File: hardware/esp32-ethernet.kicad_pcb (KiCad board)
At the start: 4 copper layers, 80 x 40 mm, 126 parts, among them J101 USB-C-2, P101 EXT_HEADER, P201 CON-SENSOR2, P202 CON-SENSOR2, P203 CON-SENSOR2, P204 CON-SENSOR2, P205 CON-SENSOR2, P206 CON-SENSOR2, P301 POE, P302 RJPSL-001TA1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

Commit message: moure routing
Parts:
- moved D104 24.5 mm to (154.3, 143.3), turned to 90 degrees
- moved R110 10.9 mm to (182.2, 127.2), turned to 90 degrees
- moved C115 10.8 mm to (181.2, 127.2), turned to 90 degrees
- moved R102 8.41 mm to (156.6, 142.5), turned to 270 degrees
- moved RP101 6.74 mm to (155.0, 146.3), turned to 0 degrees
- moved R112 5.61 mm to (153.7, 140.6), turned to 0 degrees
- moved R114 4.92 mm to (149.3, 143.1), turned to 90 degrees
- moved R1 3.40 mm to (133.7, 130.1)
- moved C306 3.30 mm to (191.4, 132.6), turned to 270 degrees
- moved R107 3.23 mm to (169.0, 150.4), turned to 90 degrees
- moved L301 1.80 mm to (185.1, 135.4)
- moved C301 1.70 mm to (182.1, 135.4)
- moved C302 1.13 mm to (179.7, 134.1)
- moved C303 1.11 mm to (189.9, 135.8)
- moved C305 1.10 mm to (182.3, 134.3)
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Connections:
- D104 pad 1: ESP_IO0_AUTO -> ESP_IO0_KEY
- D104 pad 2: ESP_IO0_KEY -> ESP_IO0_AUTO
- RP101 pad 1: B0-MISO -> B0-CLK
- RP101 pad 2: B0-CLK -> B0-MISO
- RP101 pad 7: Net-(RP101-Pad7) -> Net-(R102-Pad1)
- RP101 pad 8: Net-(R102-Pad1) -> Net-(RP101-Pad8)
- U104 pad 13: Net-(RP101-Pad7) -> Net-(RP101-Pad8)
- U104 pad 8: B-CS0 -> B-CS1
- U104 pad 9: B-CS1 -> B-CS0
- U204 pad 10: B0-CS5 -> B0-CS0
- U204 pad 11: B0-CS4 -> B0-CS1
- U204 pad 12: B0-CS3 -> B0-CS2
- U204 pad 13: B0-CS2 -> B0-CS3
- U204 pad 14: B0-CS1 -> B0-CS4
- U204 pad 15: B0-CS0 -> B0-CS5
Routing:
- net B-CS2: track 0.00 -> 36.4 mm, vias 0 -> 2
- net Net-(Q101-PadE): track 1.61 -> 32.1 mm, vias 0 -> 2
- net ESP_TXD: track 1.72 -> 26.5 mm
- net B0-CS2: track 5.79 -> 29.6 mm, vias 2 -> 3
- net B0-CS4: track 8.26 -> 31.8 mm, vias 0 -> 2
- net ESP_ADC_5V: track 1.04 -> 24.3 mm, vias 0 -> 2
- net Net-(Q102-PadE): track 2.43 -> 25.4 mm, vias 1 -> 2
- net B0-CS5: track 19.8 -> 41.9 mm, vias 2 -> 3
- net ESP_ADC_VUSB: track 1.08 -> 23.0 mm, vias 0 -> 2
- net ESP_RXD: track 2.70 -> 23.6 mm, vias 0 -> 2
- net 3V3: track 34.9 -> 55.6 mm, vias 33 -> 40
- net B0-CS3: track 21.8 -> 40.9 mm, vias 0 -> 2
- net B-CS1: track 0.00 -> 16.2 mm, vias 0 -> 2
- net Net-(P302-Pad6): track 0.00 -> 15.3 mm
- net B-CS0: track 0.00 -> 14.7 mm, vias 0 -> 2
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
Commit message: more routing
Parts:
- moved R310 0.20 mm to (177.4, 126.5)
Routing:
- net RMII_RXD1: track 0.00 -> 37.5 mm, vias 0 -> 2
- net ESP_IO0: track 0.65 -> 35.4 mm, vias 1 -> 3
- net RMII_RXD0: track 0.00 -> 34.6 mm, vias 0 -> 2
- net RMII_CRS: track 0.65 -> 33.3 mm, vias 1 -> 2
- net LED_GREEN: track 2.88 -> 27.4 mm
- net RMII_MDC: track 0.70 -> 16.9 mm, vias 1 -> 2
- net RMII_MDIO: track 0.80 -> 14.6 mm, vias 1 -> 2
- net Net-(R304-Pad1): track 1.16 -> 7.42 mm, vias 1 -> 2
- net GND: track 114.7 -> 120.6 mm, vias 119 -> 129
- net Net-(R306-Pad1): track 1.08 -> 6.58 mm, vias 1 -> 2
- net RMII_TX_EN: track 0.00 -> 3.11 mm
- net RMII_TXD0: track 0.00 -> 1.81 mm
- net RMII_TXD1: track 0.00 -> 1.61 mm
- net LED_BLUE: track 0.00 -> 1.41 mm, vias 0 -> 1

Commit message: routing finished
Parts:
- moved R315 0.64 mm to (175.5, 152.6)
- moved C312 0.50 mm to (175.5, 149.9)
- moved C313 0.50 mm to (175.5, 151.1)
- moved R316 0.50 mm to (175.5, 153.8)
- moved C303 0.20 mm to (189.9, 136.1)
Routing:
- net GND: track 120.6 -> 249.4 mm, vias 129 -> 188
- net LED_BLUE: track 1.41 -> 45.2 mm, vias 1 -> 2
- net Net-(P301-Pad3): track 0.00 -> 30.8 mm, vias 0 -> 2
- net Net-(P301-Pad4): track 0.00 -> 28.1 mm, vias 0 -> 2
- net yellowLED: track 0.58 -> 26.9 mm, vias 1 -> 2
- net Net-(P301-Pad1): track 0.00 -> 21.7 mm, vias 0 -> 2
- net ESP_EN: track 0.00 -> 17.6 mm, vias 0 -> 2
- net Net-(P301-Pad2): track 0.00 -> 15.2 mm, vias 0 -> 2
- net SHD: track 0.00 -> 14.2 mm, vias 0 -> 12
- net 3V3: track 55.6 -> 68.9 mm, vias 40 -> 49
- net LED_GREEN: track 27.4 -> 38.7 mm
- net RMII_RESET: track 1.46 -> 10.7 mm, vias 0 -> 2
- net ESP_IO0: track 35.4 -> 41.9 mm
- net Net-(C312-Pad2): track 0.00 -> 5.84 mm
- net Net-(C313-Pad2): track 0.00 -> 5.51 mm
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- added copper zone on B.Cu, net GND
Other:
- outline, holes or cut-outs redrawn

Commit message: improve layer design
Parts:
- P301: footprint kicad-libraries:pin_array_4x1 -> kicad-libraries:pin_array_5x1
- moved D101 2.90 mm to (171.8, 161.3)
- moved R115 2.90 mm to (171.8, 158.8)
- moved P301 1.20 mm to (181.1, 160.7)
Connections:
- P101 pad 6: Net-(P101-Pad6) -> GND
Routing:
- net GND: track 249.4 -> 258.8 mm, vias 188 -> 190
- net SHD: track 14.2 -> 20.8 mm
- net Net-(P301-Pad4): track 28.1 -> 29.3 mm
- net Net-(P301-Pad1): track 21.7 -> 22.8 mm
- net LED_BLUE: track 45.2 -> 44.1 mm
- net Net-(P301-Pad3): track 30.8 -> 31.8 mm
- net Net-(P301-Pad2): track 15.2 -> 16.2 mm
- net Net-(P101-Pad6): track 0.71 -> 0.00 mm
- added copper zone on F.Cu, net SHD
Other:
- board text added: "IO35 IO34 GND IO15 IO2 3V3 GND 5V"
- board text removed: "IO35 IO22 IO21 IO15 IO5 3V3 GND 5V"

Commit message: version 1.0
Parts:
- U204: value SN74LV138AD -> SN74LV138APW

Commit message: fix port description
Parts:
- added Fiducial_Mark: VAL**, kicad-libraries:Fiducial_Mark, F.Cu at (188.0, 124.8)
- added Fiducial_Mark: VAL**, kicad-libraries:Fiducial_Mark, F.Cu at (119.3, 158.7)
- added Fiducial_Mark: VAL**, kicad-libraries:Fiducial_Mark, F.Cu at (174.3, 157.7)
- added Fiducial_Mark: VAL**, kicad-libraries:Fiducial_Mark, F.Cu at (119.3, 129.7)
- added G***: LOGO, kicad-libraries:Logo_31x31, F.Cu at (135.6, 142.8)
- added VAL: CE_5mm, kicad-libraries:CE_5mm, B.Cu at (162.8, 143.7)
- added VAL: WEEE_7mm, kicad-libraries:WEEE_7mm, B.Cu at (170.8, 143.7)

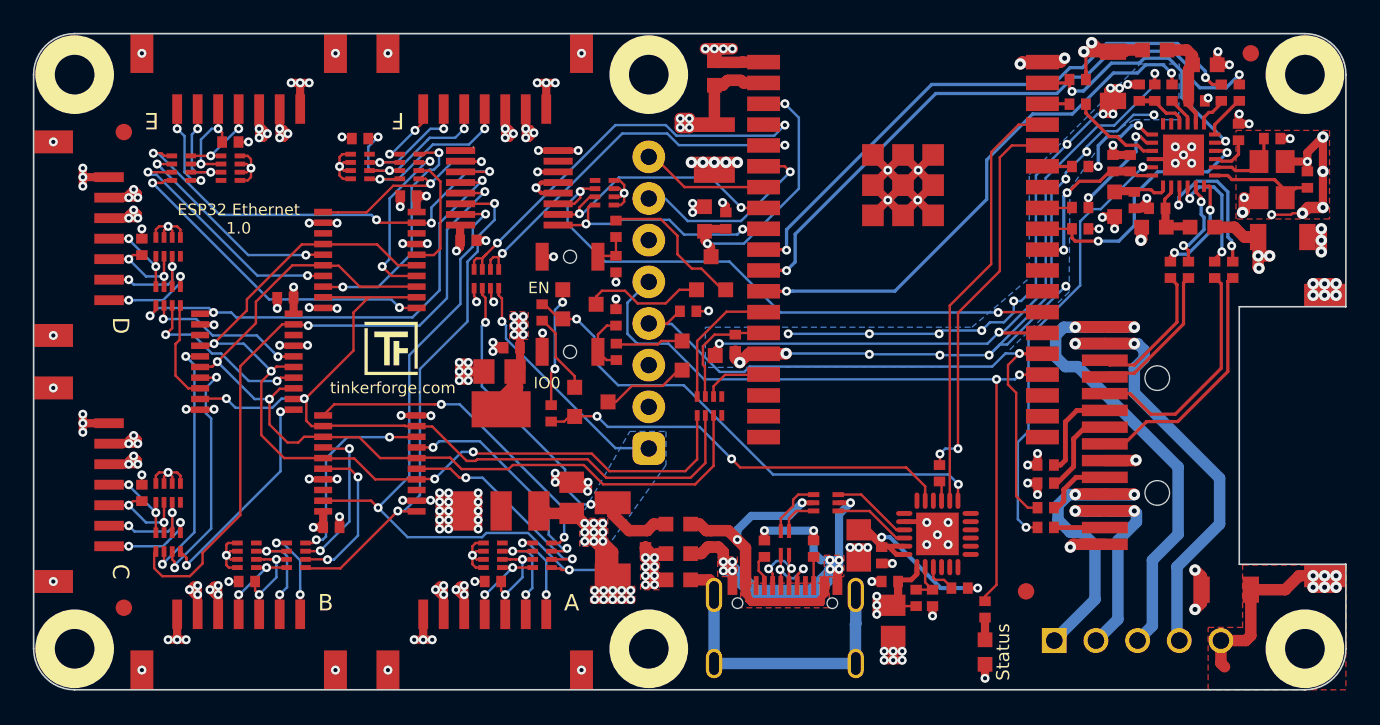
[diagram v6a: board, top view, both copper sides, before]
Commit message: version 1.1
 * change SPI pins
 * change GPIO header pinout
 * add Silkscreen
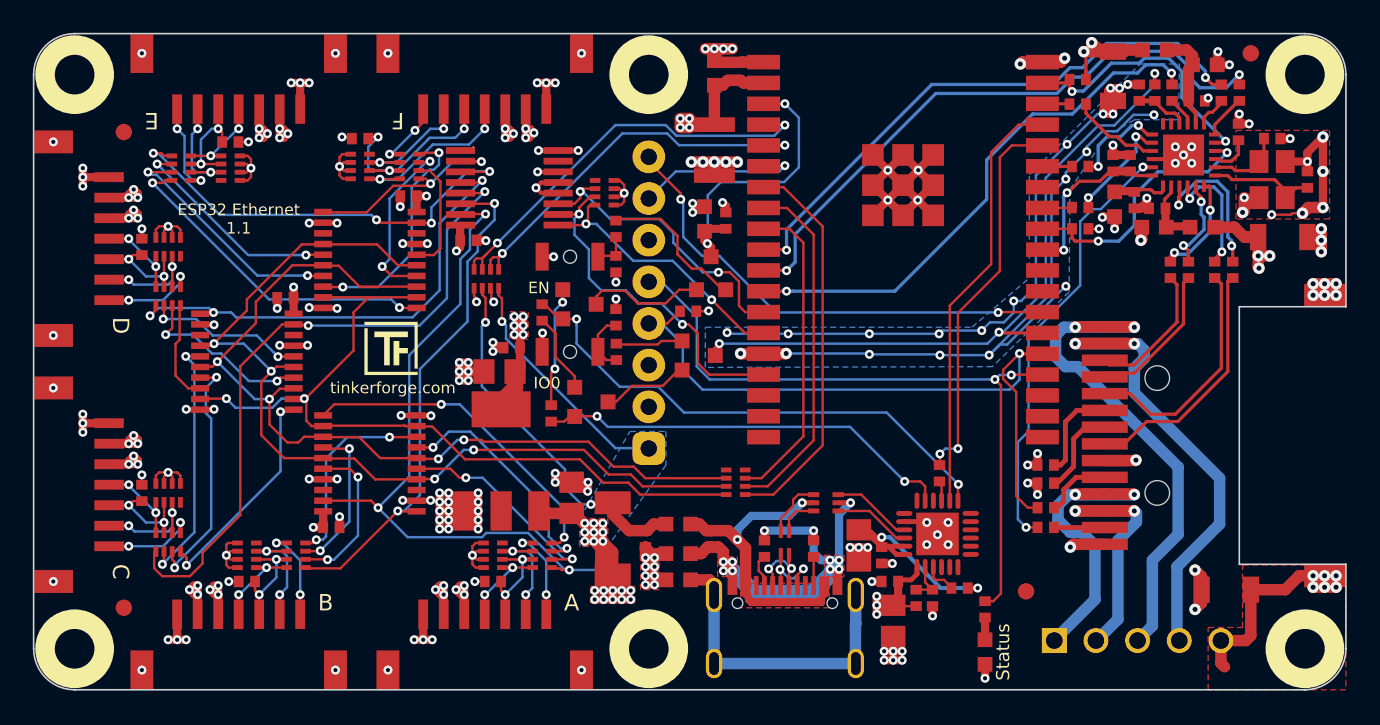
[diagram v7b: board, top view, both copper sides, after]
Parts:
- removed R102: 10k, kicad-libraries:R0402F
- U301: value KSZ80X1RNA -> KSZ8091RNAIA
- moved RP101 4.92 mm to (156.6, 151.0), turned to 90 degrees
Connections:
- P101 pad 8: ESP_IO35 -> ESP_IO4
- RP101 pad 1: B0-CLK -> Net-(RP101-Pad1)
- RP101 pad 2: B0-MISO -> Net-(RP101-Pad2)
- RP101 pad 3: B0-MOSI -> Net-(RP101-Pad3)
- RP101 pad 6: Net-(RP101-Pad6) -> B0-MOSI
- RP101 pad 7: Net-(R102-Pad1) -> B0-CLK
- RP101 pad 8: Net-(RP101-Pad8) -> B0-MISO
- U104 pad 13: Net-(RP101-Pad8) -> B-CS2
- U104 pad 14: Net-(R102-Pad1) -> B-CS0
- U104 pad 16: Net-(RP101-Pad6) -> B-CS1
- U104 pad 26: B-CS2 -> ESP_IO4
- U104 pad 7: ESP_IO35 -> Net-(RP101-Pad1)
- U104 pad 8: B-CS1 -> Net-(RP101-Pad2)
- U104 pad 9: B-CS0 -> Net-(RP101-Pad3)
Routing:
- net ESP_IO4: track 0.00 -> 29.6 mm, vias 0 -> 2
- net Net-(RP101-Pad1): track 0.00 -> 23.9 mm
- net Net-(RP101-Pad2): track 0.00 -> 21.6 mm
- net Net-(RP101-Pad3): track 0.00 -> 19.2 mm
- net B-CS2: track 36.4 -> 18.3 mm
- net Net-(RP101-Pad8): track 8.23 -> 0.00 mm
- net ESP_IO35: track 7.79 -> 0.00 mm
- net Net-(R102-Pad1): track 7.28 -> 0.00 mm
- net B-CS1: track 15.9 -> 21.5 mm
- net Net-(RP101-Pad6): track 3.97 -> 0.00 mm
- net LED_GREEN: track 38.7 -> 41.7 mm
- net GND: track 258.8 -> 261.5 mm, vias 190 -> 191
- net B0-MOSI: track 57.2 -> 54.9 mm, vias 2 -> 4
- net B-CS0: track 14.7 -> 16.9 mm
- net ESP_IO34: track 12.2 -> 10.4 mm
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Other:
- board text added: "ESP32 Ethernet 1.1"
- board text added: "GPIO"
- board text added: "IO4 IO34 GND IO15 IO2 3V3 GND 5V"
- board text added: "Input only"
- board text added: "P1"
- board text added: "P2"
- board text added: "P3"
- board text added: "P4"
- board text added: "PoE"
- board text added: "SHD"
- board text removed: "ESP32 Ethernet 1.0"
- board text removed: "IO35 IO34 GND IO15 IO2 3V3 GND 5V"

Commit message: specify ethernet ic
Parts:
- U301: value KSZ8091RNAIA -> KSZ8091RNACA
